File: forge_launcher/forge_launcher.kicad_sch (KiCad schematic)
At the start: 191 parts, among them J10 Screw_Terminal_01x02, J11 Screw_Terminal_01x02, J12 Screw_Terminal_01x02, J3 Conn_01x06, J7 Screw_Terminal_01x02, J9 Screw_Terminal_01x02, Q1 STR2P3LLH6(Pfet), Q10 MMBT3904, Q2 2N3904, Q3 MMBT3904, Q4 IPD60R145, Q6 IPD60R145, Q9 MMBT3904, SW10 LAUNCH, SW3 ARM, U1 LT3420, U10 AMC3330, U14 AMC3302, U17 AD7352, U18 IR2127, U2 TLV74318, U23 TLV74325, U3 AD7352, U4 TLV74325, U5 LMO78_03-1.0, U6 4945, U8 AMC3330

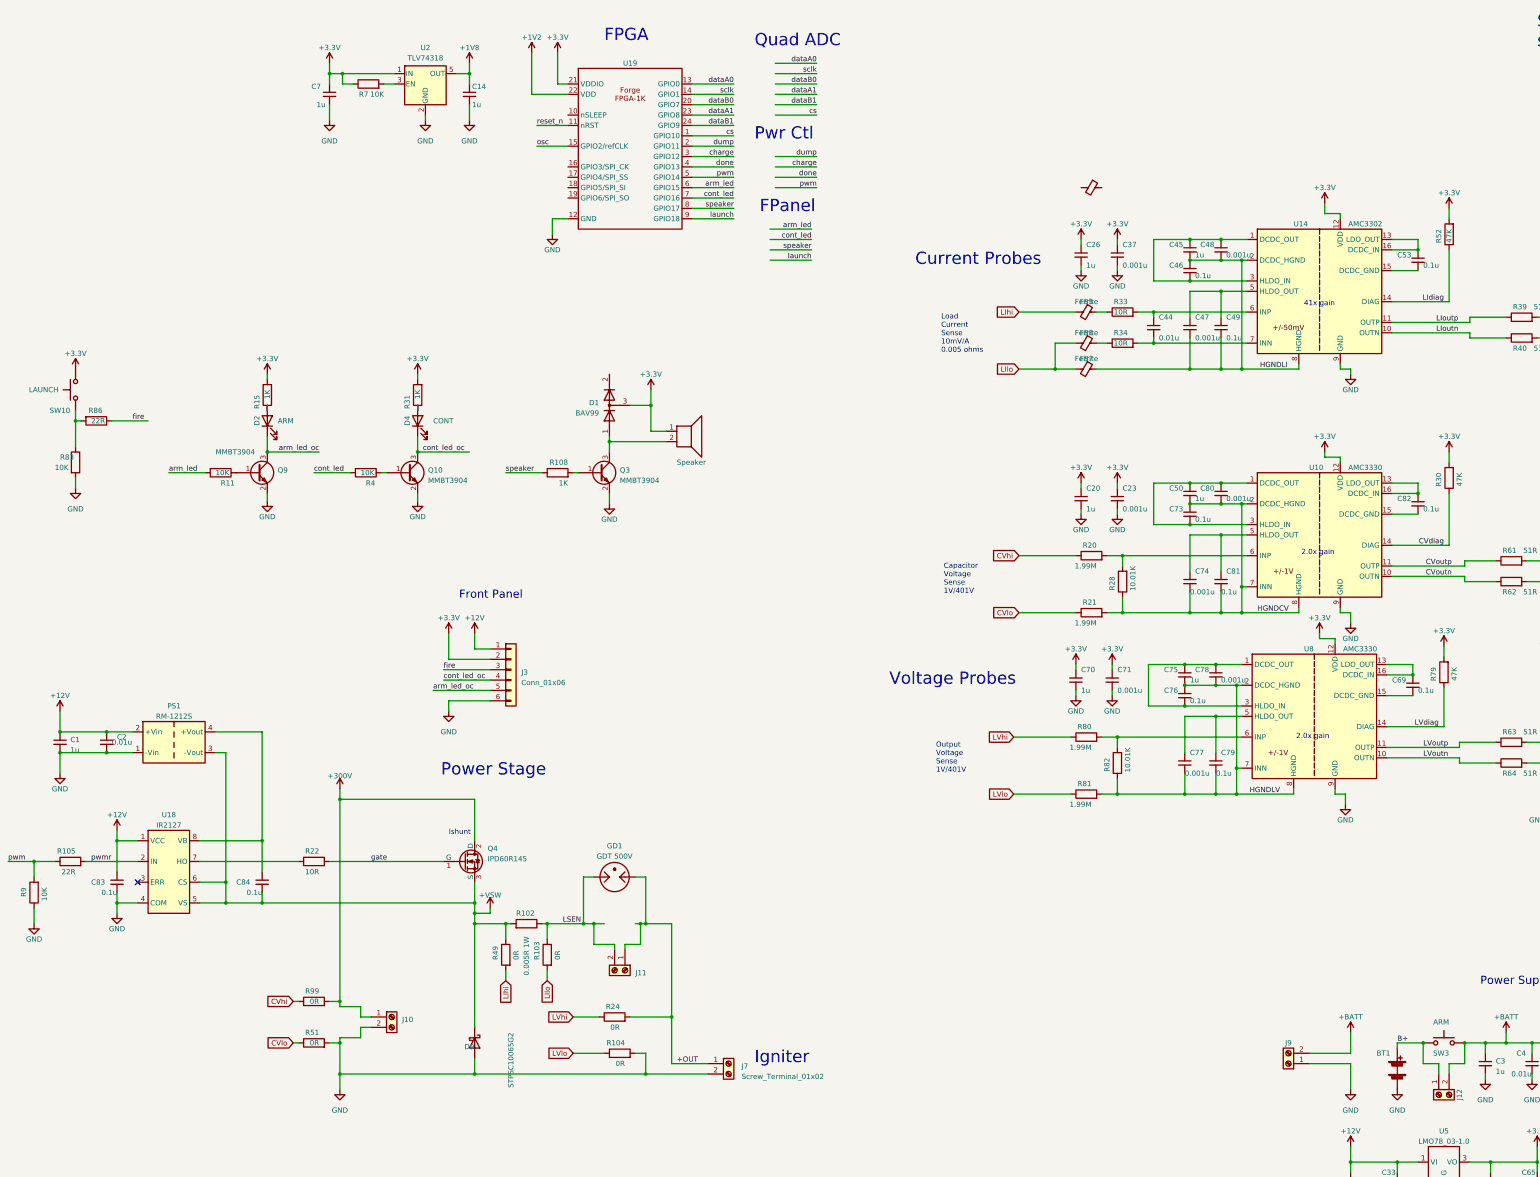
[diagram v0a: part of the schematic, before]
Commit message: handheld controller PCB layout. Caps, Coil and 4xAA battery holder on bottom side. 2 buttons, 2 leds on topside. ForgeFPGA can mount below with battery removed and 02x13 header sockets added. Will 3d print minimum volume case with buttons and lite pipes.
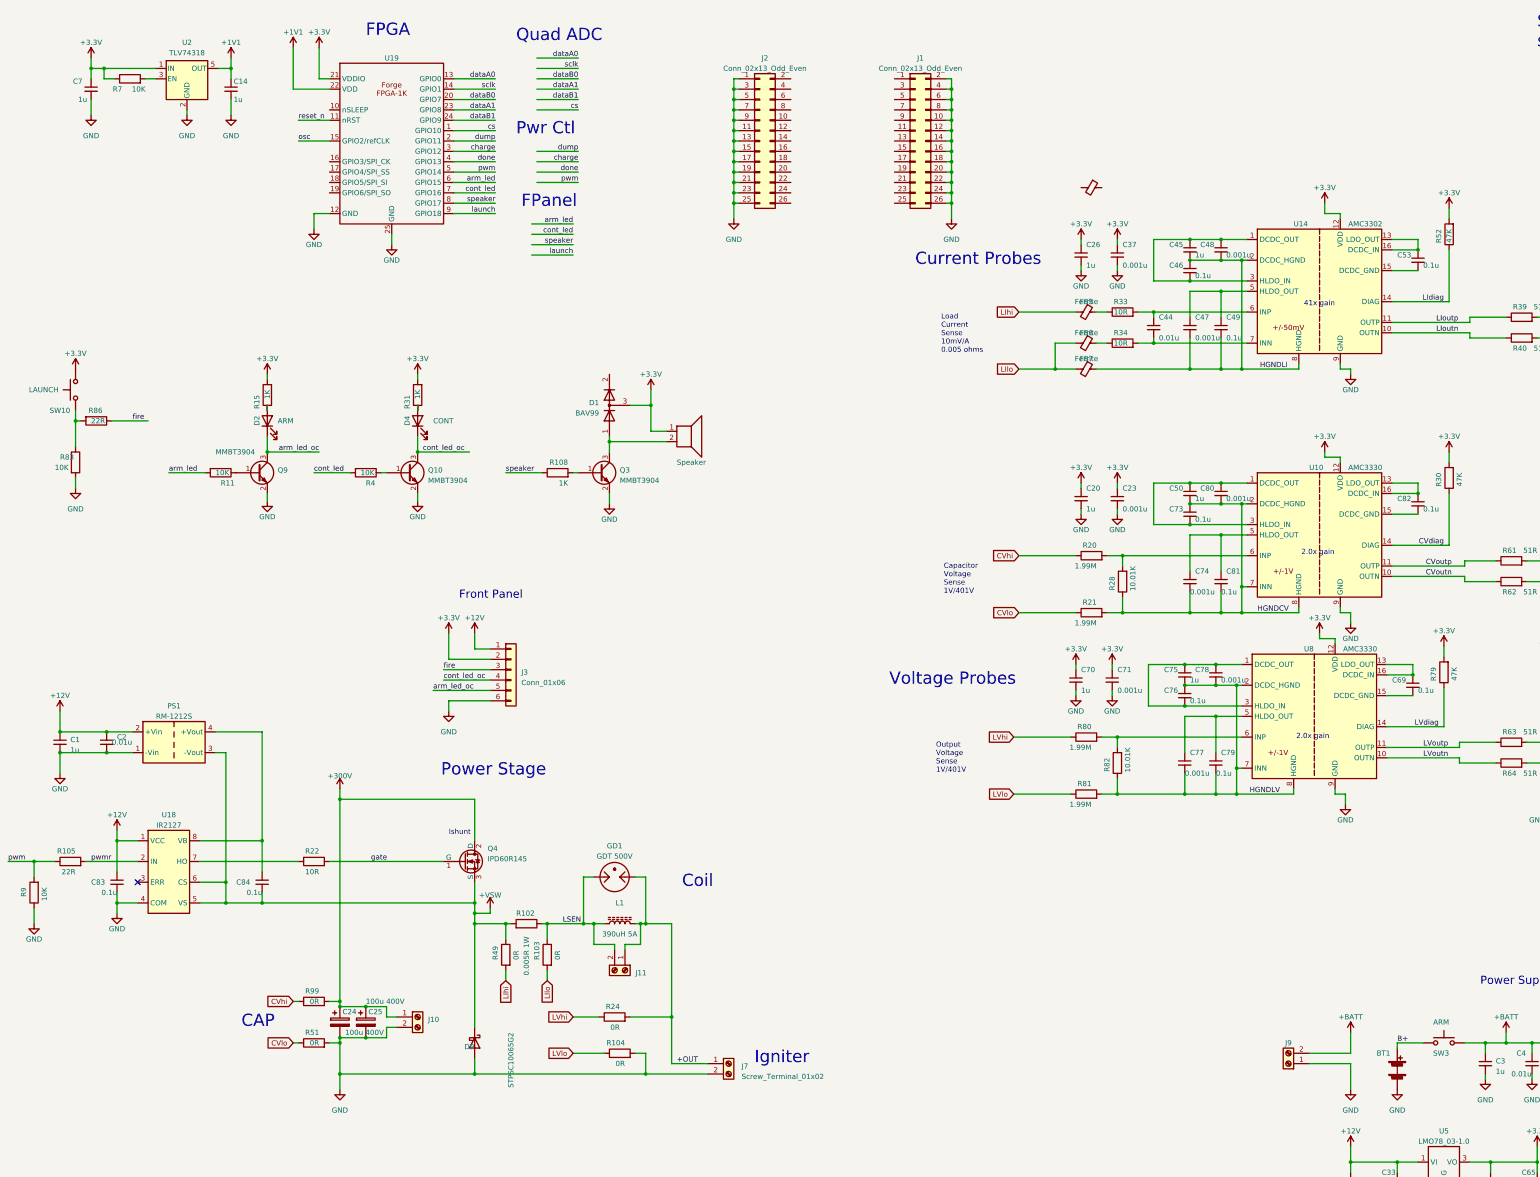
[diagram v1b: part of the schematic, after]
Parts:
- removed J12: Screw_Terminal_01x02, TerminalBlock_Phoenix:TerminalBlock_Phoenix_MKDS-1,5-2-5.08_1x02_P5.08mm_Horizontal, symbol Connector:Screw_Terminal_01x02
- added C24, C25: 100u 400V, Capacitor_THT:CP_Radial_D16.0mm_P7.50mm, symbol Device:C_Polarized
- added J1, J2: Conn_02x13_Odd_Even, symbol Connector_Generic:Conn_02x13_Odd_Even
- added L1: 390uH 5A, Inductor_THT:L_Toroid_Vertical_L35.6mm_W17.8mm_P12.70mm_Pulse_E, symbol Device:L_Ferrite
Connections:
- net +1V8 is gone; now on net +1V1: C14.1, U2.5 (OUT)
- net +300V: now also C24.1, C25.1
- net +OUT: now also L1.2
- net GND: now also U19.25 (GND), C24.2, C25.2, J1.10 (Pin_10), J1.12 (Pin_12), J1.14 (Pin_14), J1.16 (Pin_16), J1.18 (Pin_18), J1.2 (Pin_2), J1.20 (Pin_20), J1.22 (Pin_22), J1.24 (Pin_24), J1.26 (Pin_26), J1.4 (Pin_4), J1.6 (Pin_6), J1.8 (Pin_8), J2.1 (Pin_1), J2.11 (Pin_11), J2.13 (Pin_13), J2.15 (Pin_15), J2.17 (Pin_17), J2.19 (Pin_19), J2.21 (Pin_21), J2.23 (Pin_23), J2.25 (Pin_25), J2.3 (Pin_3), J2.5 (Pin_5), J2.7 (Pin_7), J2.9 (Pin_9)
- net LSEN: now also L1.1
- net +1V2 renamed +1V1
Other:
- note added: "CAP"
- note added: "Coil"
- moved on the sheet: C14, C7, J10, R7, U2

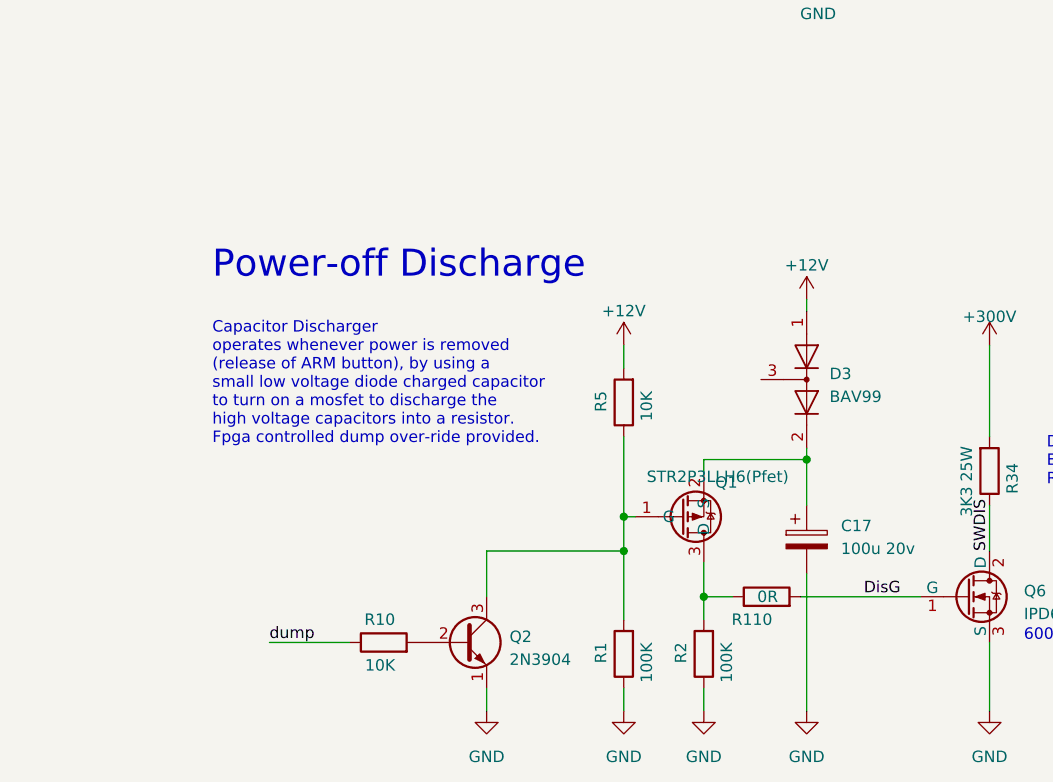
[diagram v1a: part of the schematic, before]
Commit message: Landscape style PCB initial layout 3d. Large components on bottom as per model. Forge emulator connector section of PCB can be cut away, but also has a spare fpga land point.
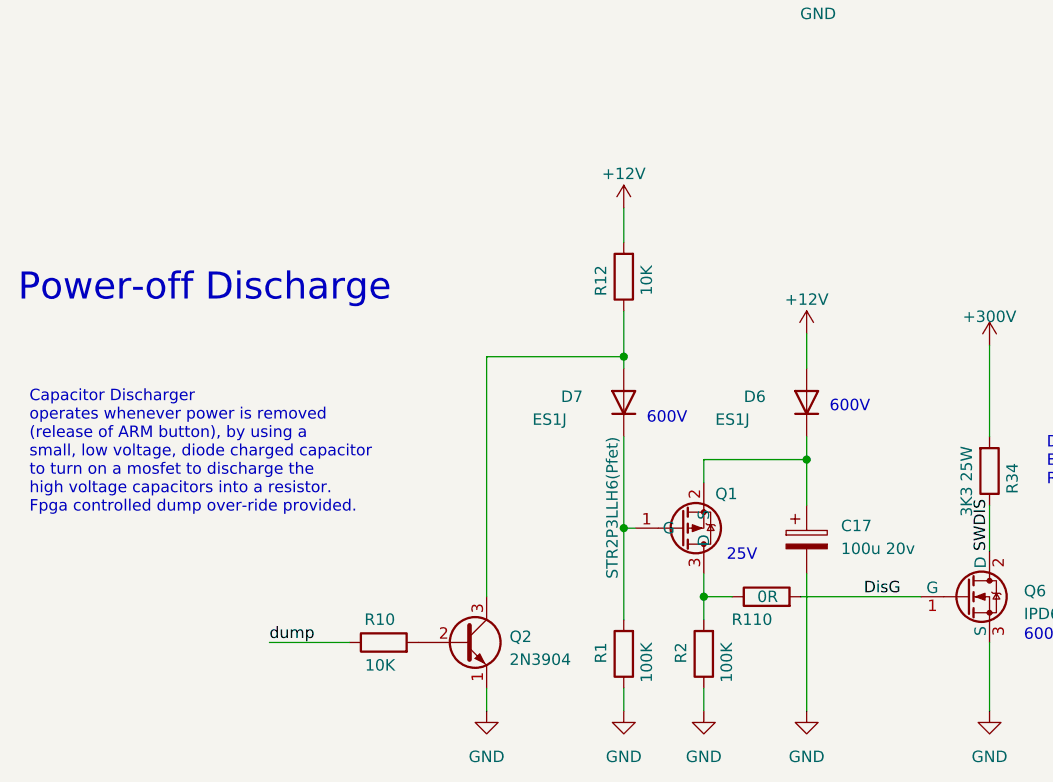
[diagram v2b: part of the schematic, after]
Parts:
- removed D3: BAV99, Package_TO_SOT_SMD:SOT-23, symbol Diode:BAV99
- removed R5: 10K, Resistor_SMD:R_0603_1608Metric, symbol Device:R
- added D6, D7: ES1J, Diode_SMD:D_SMA, symbol Diode:1N4007
- added R12: 10K, Resistor_SMD:R_0603_1608Metric, symbol Device:R
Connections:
- net +12V: now also D6.2 (A), R12.2
- net at Q1.1 (G), R1.2: now also D7.1 (K); no longer Q2.3 (C)
- net at C17.1, Q1.2 (S): now also D6.1 (K)
- new net: D7.2 (A), Q2.3 (C), R12.1
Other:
- note added: "25V"
- note added: "Capacitor Discharger operates whenever power is removed (release of ARM button), by using a small, low voltage, diode charged capacitor to turn on a mosfet to discharge the high voltage capacitors into a resistor. Fpga controlled dump over-ride provided."
- note removed: "Capacitor Discharger operates whenever power is removed (release of ARM button), by using a small low voltage diode charged capacitor to turn on a mosfet to discharge the high voltage capacitors into a resistor. Fpga controlled dump over-ride provided."
- moved on the sheet: Q1
